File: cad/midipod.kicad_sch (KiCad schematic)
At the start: 20 parts, among them IC1 ATMEGA8U2, P1 ISP, P2 USB, P3 INV1, P4 SW1, Y1 Crystal

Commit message: UPdate to KiCad 8
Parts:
- C2: symbol Device:CP1_Small -> midipod-rescue:CP1_Small-Device
- D1, D2: symbol Device:LED_Small_ALT -> midipod-rescue:LED_Small_ALT-Device

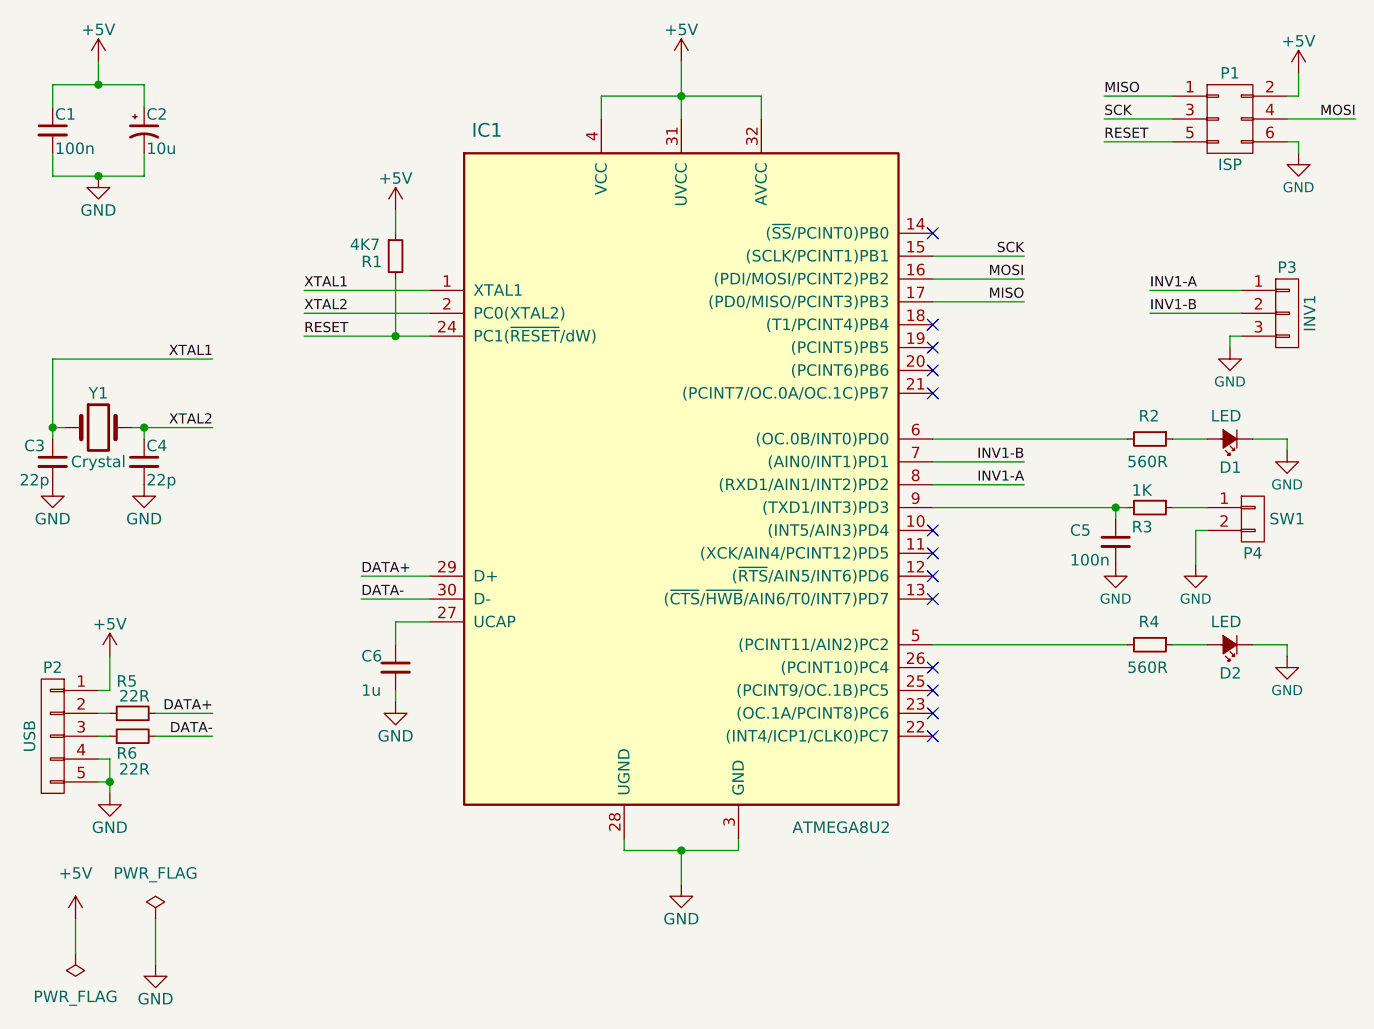
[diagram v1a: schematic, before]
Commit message: Update to KiCad 9
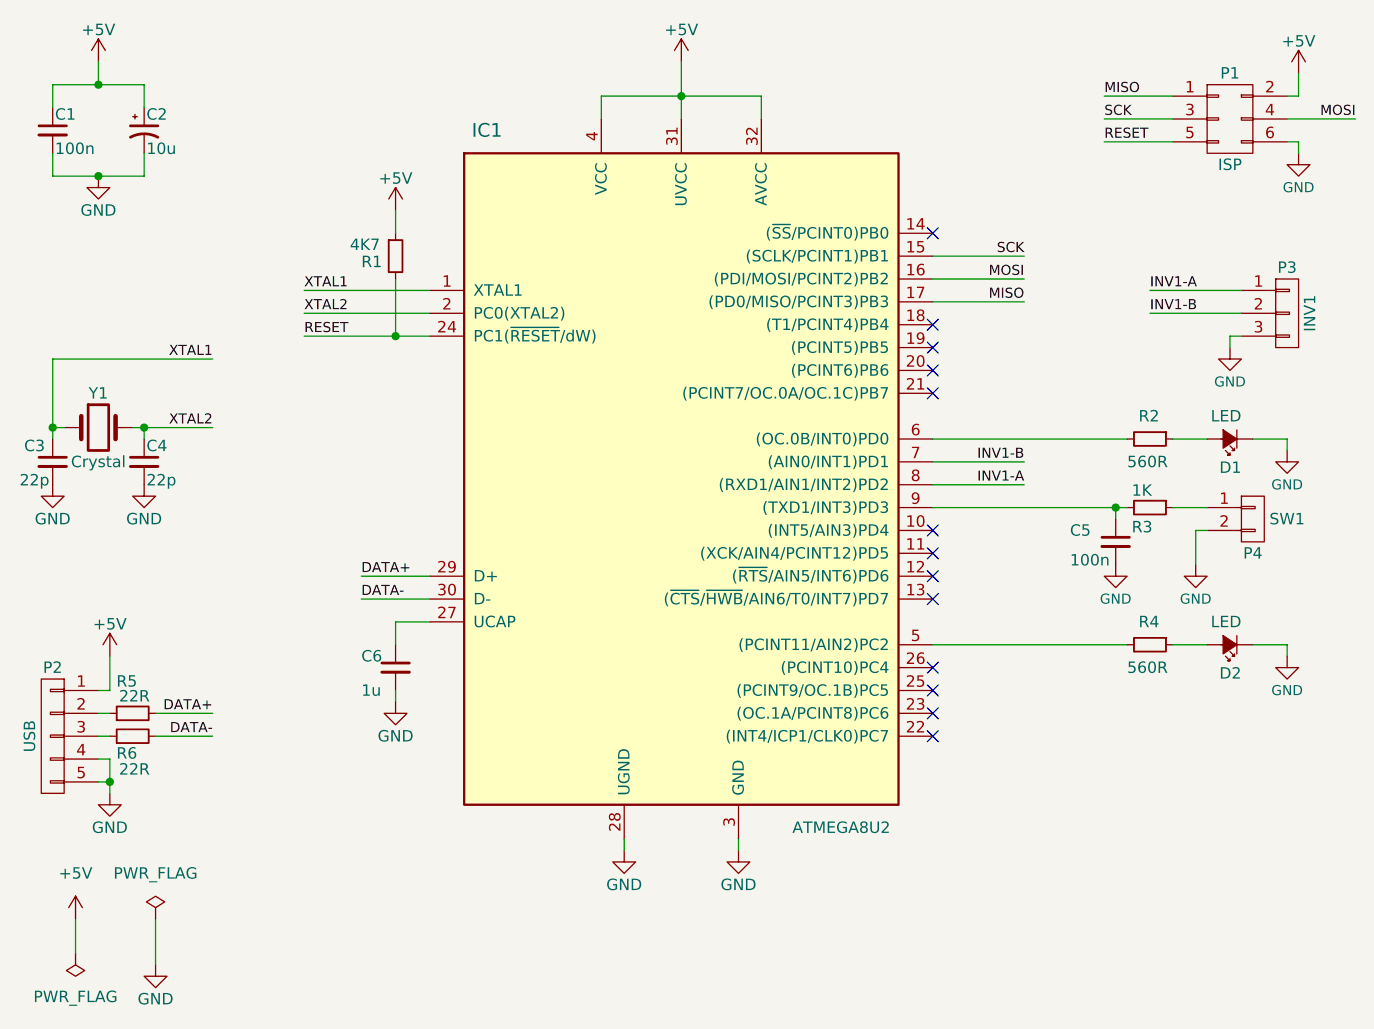
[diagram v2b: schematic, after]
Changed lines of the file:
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@@
 (kicad_sch
-	(version 20231120)
+	(version 20250114)
 	(generator "eeschema")
-	(generator_version "8.0")
+	(generator_version "9.0")
 	(paper "A4")
 	(title_block
@@
 		(color 0 0 0 0)
 	)
-	(junction
-		(at 148.59 125.73)
-		(diameter 0)
-		(color 0 0 0 0)
-	)
 	(no_connect
 		(at 176.53 105.41)
@@
 	(wire
 		(pts
-			(xy 148.59 125.73) (xy 154.94 125.73)
-		)
-		(stroke
-			(width 0)
-			(type default)
-		)
-	)
-	(wire
-		(pts
 			(xy 210.82 63.5) (xy 200.66 63.5)
 		)
@@
 	(wire
 		(pts
-			(xy 148.59 125.73) (xy 148.59 129.54)
-		)
-		(stroke
-			(width 0)
-			(type default)
-		)
-	)
-	(wire
-		(pts
 			(xy 176.53 87.63) (xy 196.85 87.63)
 		)
@@
 	(wire
 		(pts
-			(xy 142.24 125.73) (xy 148.59 125.73)
-		)
-		(stroke
-			(width 0)
-			(type default)
-		)
-	)
-	(wire
-		(pts
 			(xy 88.9 78.74) (xy 96.52 78.74)
 		)
@@
 	(symbol
 		(lib_id "midipod-rescue:GND-power")
-		(at 148.59 129.54 0)
+		(at 142.24 125.73 0)
 		(unit 1)
 		(exclude_from_sim no)
@@
 		(dnp no)
 		(property "Reference" "#PWR012"
-			(at 148.59 135.89 0)
+			(at 142.24 132.08 0)
 			(effects
 				(font
@@
 		)
 		(property "Value" "GND"
-			(at 148.59 133.35 0)
+			(at 142.24 129.54 0)
 			(effects
 				(font
@@
 		)
 		(property "Footprint" ""
-			(at 148.59 129.54 0)
+			(at 142.24 125.73 0)
 			(effects
 				(font
@@
 		)
 		(property "Datasheet" ""
-			(at 148.59 129.54 0)
+			(at 142.24 125.73 0)
 			(effects
 				(font
@@
 		)
 		(property "Description" ""
-			(at 148.59 129.54 0)
+			(at 142.24 125.73 0)
 			(effects
 				(font
@@
 		)
 	)
+	(symbol
+		(lib_id "midipod-rescue:GND-power")
+		(at 154.94 125.73 0)
+		(unit 1)
+		(exclude_from_sim no)
+		(in_bom yes)
+		(on_board yes)
+		(dnp no)
+		(property "Reference" "#PWR020"
+			(at 154.94 132.08 0)
+			(effects
+				(font
+					(size 1.27 1.27)
+				)
+				(hide yes)
+			)
+		)
+		(property "Value" "GND"
+			(at 154.94 129.54 0)
+			(effects
+				(font
+					(size 1.27 1.27)
+				)
+			)
+		)
+		(property "Footprint" ""
+			(at 154.94 125.73 0)
+			(effects
+				(font
+					(size 1.524 1.524)
+				)
+			)
+		)
+		(property "Datasheet" ""
+			(at 154.94 125.73 0)
+			(effects
+				(font
+					(size 1.524 1.524)
+				)
+			)
+		)
+		(property "Description" ""
+			(at 154.94 125.73 0)
+			(effects
+				(font
+					(size 1.27 1.27)
+				)
+				(hide yes)
+			)
+		)
+		(pin "1"
+		)
+		(instances
+			(project "midipod"
+				(path "/e6ac57a7-2771-4a34-a684-7fd0c953c8bb"
+					(reference "#PWR020")
+					(unit 1)
+				)
+			)
+		)
+	)
 	(sheet_instances
 		(path "/"
@@
 		)
 	)
+	(embedded_fonts no)
 )
